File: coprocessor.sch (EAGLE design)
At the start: 49 parts, among them IC1 MEGA32U2, J1 AVR_SPI_PRG_6NS, U1 TPS61090RSAR, U3 V_REG_LDOSMD2, U4 AZV321

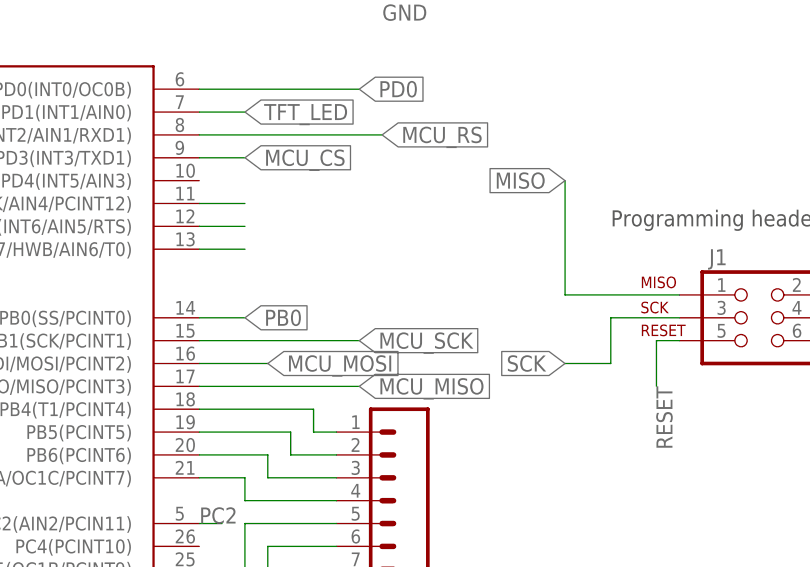
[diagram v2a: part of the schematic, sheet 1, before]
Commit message: updated the gerbers- fixed the pour and a few clearance issues.
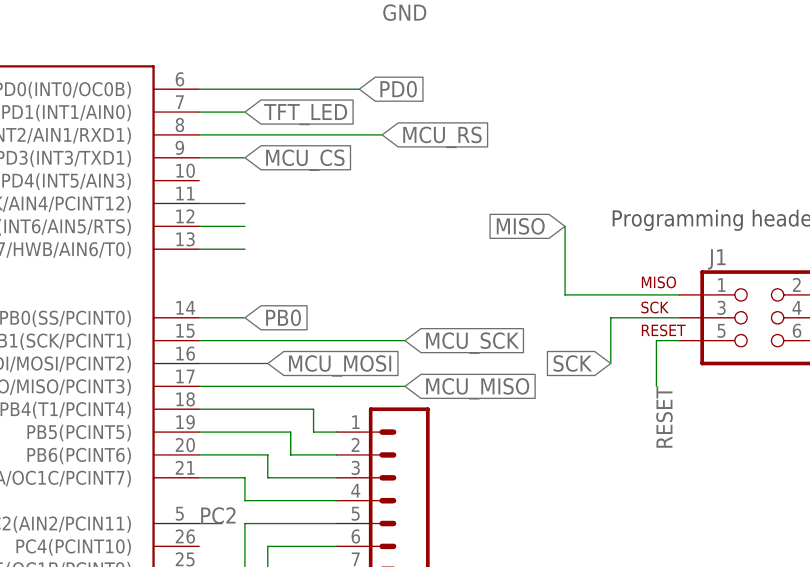
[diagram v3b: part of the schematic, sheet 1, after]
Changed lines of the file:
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@@
 <grid distance="0.1" unitdist="inch" unit="inch" style="lines" multiple="1" display="no" altdistance="0.01" altunitdist="inch" altunit="inch"/>
 <layers>
-<layer number="1" name="Top" color="4" fill="1" visible="yes" active="no"/>
-<layer number="2" name="Route2" color="1" fill="3" visible="yes" active="no"/>
-<layer number="3" name="Route3" color="4" fill="3" visible="yes" active="no"/>
-<layer number="14" name="Route14" color="1" fill="6" visible="yes" active="no"/>
-<layer number="15" name="Route15" color="4" fill="6" visible="yes" active="no"/>
-<layer number="16" name="Bottom" color="1" fill="1" visible="yes" active="no"/>
-<layer number="17" name="Pads" color="2" fill="1" visible="yes" active="no"/>
-<layer number="18" name="Vias" color="2" fill="1" visible="yes" active="no"/>
-<layer number="19" name="Unrouted" color="6" fill="1" visible="yes" active="no"/>
-<layer number="20" name="Dimension" color="15" fill="1" visible="yes" active="no"/>
-<layer number="21" name="tPlace" color="7" fill="1" visible="yes" active="no"/>
-<layer number="22" name="bPlace" color="7" fill="1" visible="yes" active="no"/>
-<layer number="23" name="tOrigins" color="15" fill="1" visible="yes" active="no"/>
-<layer number="24" name="bOrigins" color="15" fill="1" visible="yes" active="no"/>
-<layer number="25" name="tNames" color="7" fill="1" visible="yes" active="no"/>
-<layer number="26" name="bNames" color="7" fill="1" visible="yes" active="no"/>
-<layer number="27" name="tValues" color="7" fill="1" visible="yes" active="no"/>
-<layer number="28" name="bValues" color="7" fill="1" visible="yes" active="no"/>
+<layer number="1" name="Top" color="4" fill="1" visible="no" active="no"/>
+<layer number="2" name="Route2" color="1" fill="3" visible="no" active="no"/>
+<layer number="3" name="Route3" color="4" fill="3" visible="no" active="no"/>
+<layer number="14" name="Route14" color="1" fill="6" visible="no" active="no"/>
+<layer number="15" name="Route15" color="4" fill="6" visible="no" active="no"/>
+<layer number="16" name="Bottom" color="1" fill="1" visible="no" active="no"/>
+<layer number="17" name="Pads" color="2" fill="1" visible="no" active="no"/>
+<layer number="18" name="Vias" color="2" fill="1" visible="no" active="no"/>
+<layer number="19" name="Unrouted" color="6" fill="1" visible="no" active="no"/>
+<layer number="20" name="Dimension" color="15" fill="1" visible="no" active="no"/>
+<layer number="21" name="tPlace" color="7" fill="1" visible="no" active="no"/>
+<layer number="22" name="bPlace" color="7" fill="1" visible="no" active="no"/>
+<layer number="23" name="tOrigins" color="15" fill="1" visible="no" active="no"/>
+<layer number="24" name="bOrigins" color="15" fill="1" visible="no" active="no"/>
+<layer number="25" name="tNames" color="7" fill="1" visible="no" active="no"/>
+<layer number="26" name="bNames" color="7" fill="1" visible="no" active="no"/>
+<layer number="27" name="tValues" color="7" fill="1" visible="no" active="no"/>
+<layer number="28" name="bValues" color="7" fill="1" visible="no" active="no"/>
 <layer number="29" name="tStop" color="7" fill="3" visible="no" active="no"/>
 <layer number="30" name="bStop" color="7" fill="6" visible="no" active="no"/>
@@
 <layer number="35" name="tGlue" color="7" fill="4" visible="no" active="no"/>
 <layer number="36" name="bGlue" color="7" fill="5" visible="no" active="no"/>
-<layer number="37" name="tTest" color="7" fill="1" visible="yes" active="no"/>
-<layer number="38" name="bTest" color="7" fill="1" visible="yes" active="no"/>
+<layer number="37" name="tTest" color="7" fill="1" visible="no" active="no"/>
+<layer number="38" name="bTest" color="7" fill="1" visible="no" active="no"/>
 <layer number="39" name="tKeepout" color="4" fill="11" visible="no" active="no"/>
 <layer number="40" name="bKeepout" color="1" fill="11" visible="no" active="no"/>
@@
 <layer number="44" name="Drills" color="7" fill="1" visible="no" active="no"/>
 <layer number="45" name="Holes" color="7" fill="1" visible="no" active="no"/>
-<layer number="46" name="Milling" color="3" fill="1" visible="yes" active="no"/>
-<layer number="47" name="Measures" color="7" fill="1" visible="yes" active="no"/>
-<layer number="48" name="Document" color="7" fill="1" visible="yes" active="no"/>
-<layer number="49" name="Reference" color="7" fill="1" visible="yes" active="no"/>
-<layer number="50" name="dxf" color="7" fill="1" visible="yes" active="no"/>
-<layer number="51" name="tDocu" color="7" fill="1" visible="yes" active="no"/>
-<layer number="52" name="bDocu" color="7" fill="1" visible="yes" active="no"/>
-<layer number="53" name="tGND_GNDA" color="7" fill="9" visible="yes" active="no"/>
-<layer number="54" name="bGND_GNDA" color="1" fill="9" visible="yes" active="no"/>
-<layer number="56" name="wert" color="7" fill="1" visible="yes" active="no"/>
-<layer number="57" name="tCAD" color="7" fill="1" visible="yes" active="no"/>
-<layer number="59" name="tCarbon" color="7" fill="1" visible="yes" active="no"/>
-<layer number="60" name="bCarbon" color="7" fill="1" visible="yes" active="no"/>
+<layer number="46" name="Milling" color="3" fill="1" visible="no" active="no"/>
+<layer number="47" name="Measures" color="7" fill="1" visible="no" active="no"/>
+<layer number="48" name="Document" color="7" fill="1" visible="no" active="no"/>
+<layer number="49" name="Reference" color="7" fill="1" visible="no" active="no"/>
+<layer number="50" name="dxf" color="7" fill="1" visible="no" active="no"/>
+<layer number="51" name="tDocu" color="7" fill="1" visible="no" active="no"/>
+<layer number="52" name="bDocu" color="7" fill="1" visible="no" active="no"/>
+<layer number="53" name="tGND_GNDA" color="7" fill="9" visible="no" active="no"/>
+<layer number="54" name="bGND_GNDA" color="1" fill="9" visible="no" active="no"/>
+<layer number="56" name="wert" color="7" fill="1" visible="no" active="no"/>
+<layer number="57" name="tCAD" color="7" fill="1" visible="no" active="no"/>
+<layer number="59" name="tCarbon" color="7" fill="1" visible="no" active="no"/>
+<layer number="60" name="bCarbon" color="7" fill="1" visible="no" active="no"/>
 <layer number="90" name="Modules" color="5" fill="1" visible="yes" active="yes"/>
 <layer number="91" name="Nets" color="2" fill="1" visible="yes" active="yes"/>
@@
 <wire x1="139.7" y1="48.26" x2="132.08" y2="48.26" width="0.1524" layer="91"/>
 <wire x1="132.08" y1="48.26" x2="132.08" y2="43.18" width="0.1524" layer="91"/>
-<wire x1="132.08" y1="43.18" x2="127" y2="43.18" width="0.1524" layer="91"/>
-<label x="127" y="43.18" size="1.778" layer="95" rot="MR0" xref="yes"/>
+<label x="132.08" y="43.18" size="1.778" layer="95" rot="MR0" xref="yes"/>
 </segment>
 <segment>
@@
 <pinref part="J1" gate="G$1" pin="1"/>
 <wire x1="139.7" y1="50.8" x2="127" y2="50.8" width="0.1524" layer="91"/>
-<label x="127" y="63.5" size="1.778" layer="95" rot="MR0" xref="yes"/>
-<wire x1="127" y1="50.8" x2="127" y2="63.5" width="0.1524" layer="91"/>
+<label x="127" y="58.42" size="1.778" layer="95" rot="MR0" xref="yes"/>
+<wire x1="127" y1="50.8" x2="127" y2="58.42" width="0.1524" layer="91"/>
 </segment>
 <segment>
@@
 <segment>
 <pinref part="IC1" gate="G$1" pin="PB1(SCK/PCINT1)"/>
-<wire x1="86.36" y1="45.72" x2="104.14" y2="45.72" width="0.1524" layer="91"/>
-<label x="104.14" y="45.72" size="1.778" layer="95" xref="yes"/>
+<wire x1="86.36" y1="45.72" x2="109.22" y2="45.72" width="0.1524" layer="91"/>
+<label x="109.22" y="45.72" size="1.778" layer="95" xref="yes"/>
 </segment>
 </net>
@@
 <segment>
 <pinref part="IC1" gate="G$1" pin="PB3(PDO/MISO/PCINT3)"/>
-<wire x1="86.36" y1="40.64" x2="104.14" y2="40.64" width="0.1524" layer="91"/>
-<label x="104.14" y="40.64" size="1.778" layer="95" xref="yes"/>
-</segment>
-</net>
+<wire x1="86.36" y1="40.64" x2="109.22" y2="40.64" width="0.1524" layer="91"/>
+<label x="109.22" y="40.64" size="1.778" layer="95" xref="yes"/>
+</segment>
+</net>

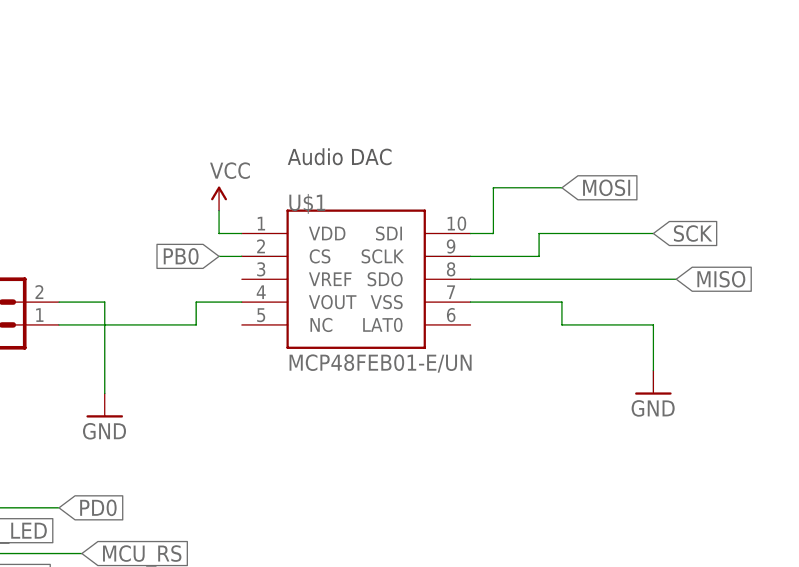
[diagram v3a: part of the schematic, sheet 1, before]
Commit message: updated the crystal layout
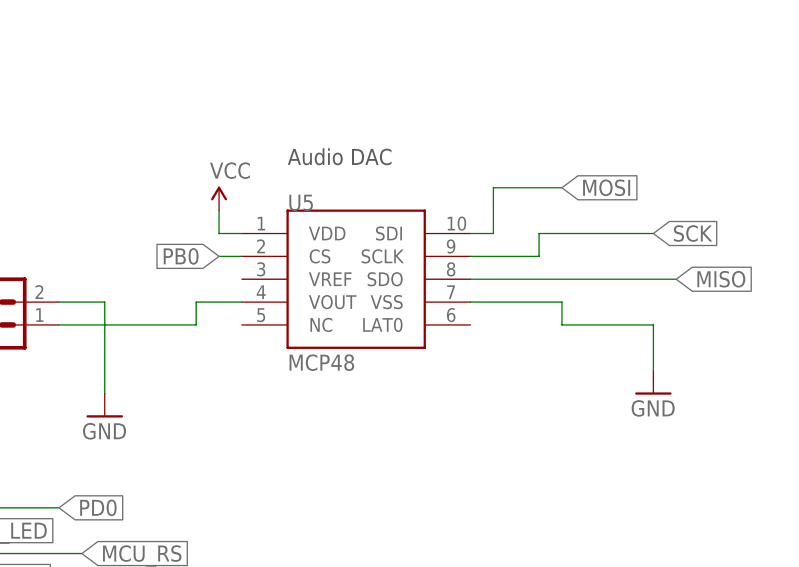
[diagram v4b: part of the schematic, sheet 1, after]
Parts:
- U5: value MCP48FEB01-E/UN -> MCP48
- renumbered U$1 to U5, U$2 to U6, U$3 to U7
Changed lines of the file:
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@@
 <part name="C4" library="SparkFun-Capacitors" deviceset="CAP_POL" device="1206" value="10uF"/>
 <part name="SUPPLY7" library="SparkFun-Aesthetics" deviceset="VCC" device=""/>
-<part name="U$1" library="custom" deviceset="MCP48FEB01-E" device="/UN"/>
+<part name="U5" library="custom" deviceset="MCP48FEB01-E" device="/UN" value="MCP48"/>
 <part name="GND9" library="SparkFun-Aesthetics" deviceset="GND" device=""/>
 <part name="J4" library="SparkFun-Connectors" deviceset="M02" device="LOCK"/>
 <part name="GND10" library="SparkFun-Aesthetics" deviceset="GND" device=""/>
-<part name="U$2" library="custom" deviceset="CRYSTAL-ABLS" device="" value="16MHZ"/>
+<part name="U6" library="custom" deviceset="CRYSTAL-ABLS" device="" value="16MHZ"/>
 <part name="R4" library="SparkFun-Resistors" deviceset="340OHM-1/10W-1%(0603)" device="" value="340k"/>
 <part name="R5" library="SparkFun-Resistors" deviceset="1.8KOHM1/10W1%(0603)" device="" value="1.87M"/>
@@
 <part name="GND25" library="SparkFun-Aesthetics" deviceset="GND" device=""/>
 <part name="TFT1" library="custom" deviceset="TFT-18-1.0MM" device=""/>
-<part name="U$3" library="custom" deviceset="CBT3244AD" device=""/>
+<part name="U7" library="custom" deviceset="CBT3244AD" device=""/>
 <part name="SUPPLY1" library="SparkFun-Aesthetics" deviceset="VCC" device=""/>
 <part name="GND28" library="SparkFun-Aesthetics" deviceset="GND" device=""/>
@@
 <instance part="C4" gate="G$1" x="48.26" y="116.84"/>
 <instance part="SUPPLY7" gate="G$1" x="121.92" y="106.68"/>
-<instance part="U$1" gate="G$1" x="137.16" y="99.06"/>
+<instance part="U5" gate="G$1" x="137.16" y="99.06"/>
 <instance part="GND9" gate="1" x="170.18" y="86.36"/>
 <instance part="J4" gate="G$1" x="96.52" y="93.98"/>
 <instance part="GND10" gate="1" x="109.22" y="83.82"/>
-<instance part="U$2" gate="G$1" x="12.7" y="38.1" rot="R90"/>
+<instance part="U6" gate="G$1" x="12.7" y="38.1" rot="R90"/>
 <instance part="TFT1" gate="TFT$1" x="63.5" y="-5.08"/>
-<instance part="U$3" gate="G$1" x="-40.64" y="99.06"/>
+<instance part="U7" gate="G$1" x="-40.64" y="99.06"/>
 <instance part="SUPPLY1" gate="G$1" x="-20.32" y="111.76"/>
 <instance part="GND28" gate="1" x="-58.42" y="81.28"/>
@@
 </segment>
 <segment>
-<pinref part="U$1" gate="G$1" pin="VSS"/>
+<pinref part="U5" gate="G$1" pin="VSS"/>
 <wire x1="149.86" y1="96.52" x2="160.02" y2="96.52" width="0.1524" layer="91"/>
 <wire x1="160.02" y1="96.52" x2="160.02" y2="93.98" width="0.1524" layer="91"/>
@@
 </segment>
 <segment>
-<pinref part="U$3" gate="G$1" pin="GND"/>
+<pinref part="U7" gate="G$1" pin="GND"/>
 <pinref part="GND28" gate="1" pin="GND"/>
 <wire x1="-55.88" y1="86.36" x2="-58.42" y2="86.36" width="0.1524" layer="91"/>
@@
 <wire x1="124.46" y1="104.14" x2="121.92" y2="104.14" width="0.1524" layer="91"/>
 <wire x1="121.92" y1="104.14" x2="121.92" y2="106.68" width="0.1524" layer="91"/>
-<pinref part="U$1" gate="G$1" pin="VDD"/>
-</segment>
-<segment>
-<pinref part="U$3" gate="G$1" pin="VCC"/>
+<pinref part="U5" gate="G$1" pin="VDD"/>
+</segment>
+<segment>
+<pinref part="U7" gate="G$1" pin="VCC"/>
 <wire x1="-25.4" y1="109.22" x2="-20.32" y2="109.22" width="0.1524" layer="91"/>
 <pinref part="SUPPLY1" gate="G$1" pin="VCC"/>
@@
 <pinref part="C2" gate="G$1" pin="1"/>
 <wire x1="27.94" y1="43.18" x2="12.7" y2="43.18" width="0.1524" layer="91"/>
-<pinref part="U$2" gate="G$1" pin="P$2"/>
+<pinref part="U6" gate="G$1" pin="P$2"/>
 <wire x1="12.7" y1="43.18" x2="0" y2="43.18" width="0.1524" layer="91"/>
 <junction x="12.7" y="43.18"/>
@@
 <wire x1="12.7" y1="33.02" x2="27.94" y2="35.56" width="0.1524" layer="91"/>
 <wire x1="7.62" y1="33.02" x2="7.62" y2="30.48" width="0.1524" layer="91"/>
-<pinref part="U$2" gate="G$1" pin="P$1"/>
+<pinref part="U6" gate="G$1" pin="P$1"/>
 <junction x="12.7" y="33.02"/>
 </segment>
@@
 </segment>
 <segment>
-<pinref part="U$1" gate="G$1" pin="CS"/>
+<pinref part="U5" gate="G$1" pin="CS"/>
 <wire x1="124.46" y1="101.6" x2="121.92" y2="101.6" width="0.1524" layer="91"/>
 <label x="121.92" y="101.6" size="1.778" layer="95" rot="MR0" xref="yes"/>
@@
 </segment>
 <segment>
-<pinref part="U$1" gate="G$1" pin="SCLK"/>
+<pinref part="U5" gate="G$1" pin="SCLK"/>
 <wire x1="149.86" y1="101.6" x2="157.48" y2="101.6" width="0.1524" layer="91"/>
 <wire x1="157.48" y1="101.6" x2="157.48" y2="104.14" width="0.1524" layer="91"/>
@@
 </segment>
 <segment>
-<pinref part="U$3" gate="G$1" pin="1B2"/>
+<pinref part="U7" gate="G$1" pin="1B2"/>
 <wire x1="-25.4" y1="99.06" x2="-15.24" y2="99.06" width="0.1524" layer="91"/>
 <label x="-15.24" y="99.06" size="1.778" layer="95" xref="yes"/>
@@
 </segment>
 <segment>
-<pinref part="U$1" gate="G$1" pin="SDO"/>
+<pinref part="U5" gate="G$1" pin="SDO"/>
 <wire x1="149.86" y1="99.06" x2="172.72" y2="99.06" width="0.1524" layer="91"/>
 <label x="172.72" y="99.06" size="1.778" layer="95" xref="yes"/>
@@
 </segment>
 <segment>
-<pinref part="U$1" gate="G$1" pin="SDI"/>
+<pinref part="U5" gate="G$1" pin="SDI"/>
 <wire x1="149.86" y1="104.14" x2="152.4" y2="104.14" width="0.1524" layer="91"/>
 <wire x1="152.4" y1="104.14" x2="152.4" y2="109.22" width="0.1524" layer="91"/>
@@
 </segment>
 <segment>
-<pinref part="U$3" gate="G$1" pin="1B3"/>
+<pinref part="U7" gate="G$1" pin="1B3"/>
 <wire x1="-25.4" y1="93.98" x2="-15.24" y2="93.98" width="0.1524" layer="91"/>
 <label x="-15.24" y="93.98" size="1.778" layer="95" xref="yes"/>
@@
 <net name="DAC_VOUT" class="0">
 <segment>
-<pinref part="U$1" gate="G$1" pin="VOUT"/>
+<pinref part="U5" gate="G$1" pin="VOUT"/>
 <wire x1="124.46" y1="96.52" x2="119.38" y2="96.52" width="0.1524" layer="91"/>
 <wire x1="119.38" y1="96.52" x2="119.38" y2="93.98" width="0.1524" layer="91"/>
@@
 <net name="MCU_CS" class="0">
 <segment>
-<pinref part="U$3" gate="G$1" pin="1A1"/>
+<pinref part="U7" gate="G$1" pin="1A1"/>
 <wire x1="-55.88" y1="106.68" x2="-63.5" y2="106.68" width="0.1524" layer="91"/>
 <label x="-63.5" y="106.68" size="1.778" layer="95" rot="MR0" xref="yes"/>
@@
 <net name="MCU_SCK" class="0">
 <segment>
-<pinref part="U$3" gate="G$1" pin="1A2"/>
+<pinref part="U7" gate="G$1" pin="1A2"/>
 <wire x1="-55.88" y1="101.6" x2="-63.5" y2="101.6" width="0.1524" layer="91"/>
 <label x="-63.5" y="101.6" size="1.778" layer="95" rot="MR0" xref="yes"/>
@@
 <net name="MCU_MOSI" class="0">
 <segment>
-<pinref part="U$3" gate="G$1" pin="1A3"/>
+<pinref part="U7" gate="G$1" pin="1A3"/>
 <wire x1="-55.88" y1="96.52" x2="-63.5" y2="96.52" width="0.1524" layer="91"/>
 <label x="-63.5" y="96.52" size="1.778" layer="95" rot="MR0" xref="yes"/>
@@
 <net name="MCU_RS" class="0">
 <segment>
-<pinref part="U$3" gate="G$1" pin="1A4"/>
+<pinref part="U7" gate="G$1" pin="1A4"/>
 <wire x1="-55.88" y1="91.44" x2="-63.5" y2="91.44" width="0.1524" layer="91"/>
 <label x="-63.5" y="91.44" size="1.778" layer="95" rot="MR0" xref="yes"/>
@@
 <net name="PC2" class="0">
 <segment>
-<pinref part="U$3" gate="G$1" pin="!1OE"/>
+<pinref part="U7" gate="G$1" pin="!1OE"/>
 <wire x1="-55.88" y1="109.22" x2="-63.5" y2="109.22" width="0.1524" layer="91"/>
 <label x="-71.12" y="114.3" size="1.778" layer="95" rot="R180" xref="yes"/>
@@
 </segment>
 <segment>
-<pinref part="U$3" gate="G$1" pin="1B4"/>
+<pinref part="U7" gate="G$1" pin="1B4"/>
 <wire x1="-25.4" y1="88.9" x2="-15.24" y2="88.9" width="0.1524" layer="91"/>
 <label x="-15.24" y="88.9" size="1.778" layer="95" xref="yes"/>
@@
 </segment>
 <segment>
-<pinref part="U$3" gate="G$1" pin="1B1"/>
+<pinref part="U7" gate="G$1" pin="1B1"/>
 <wire x1="-25.4" y1="104.14" x2="-17.78" y2="104.14" width="0.1524" layer="91"/>
 <label x="-17.78" y="104.14" size="1.778" layer="95" xref="yes"/>
